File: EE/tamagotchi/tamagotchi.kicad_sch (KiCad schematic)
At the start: 0 parts

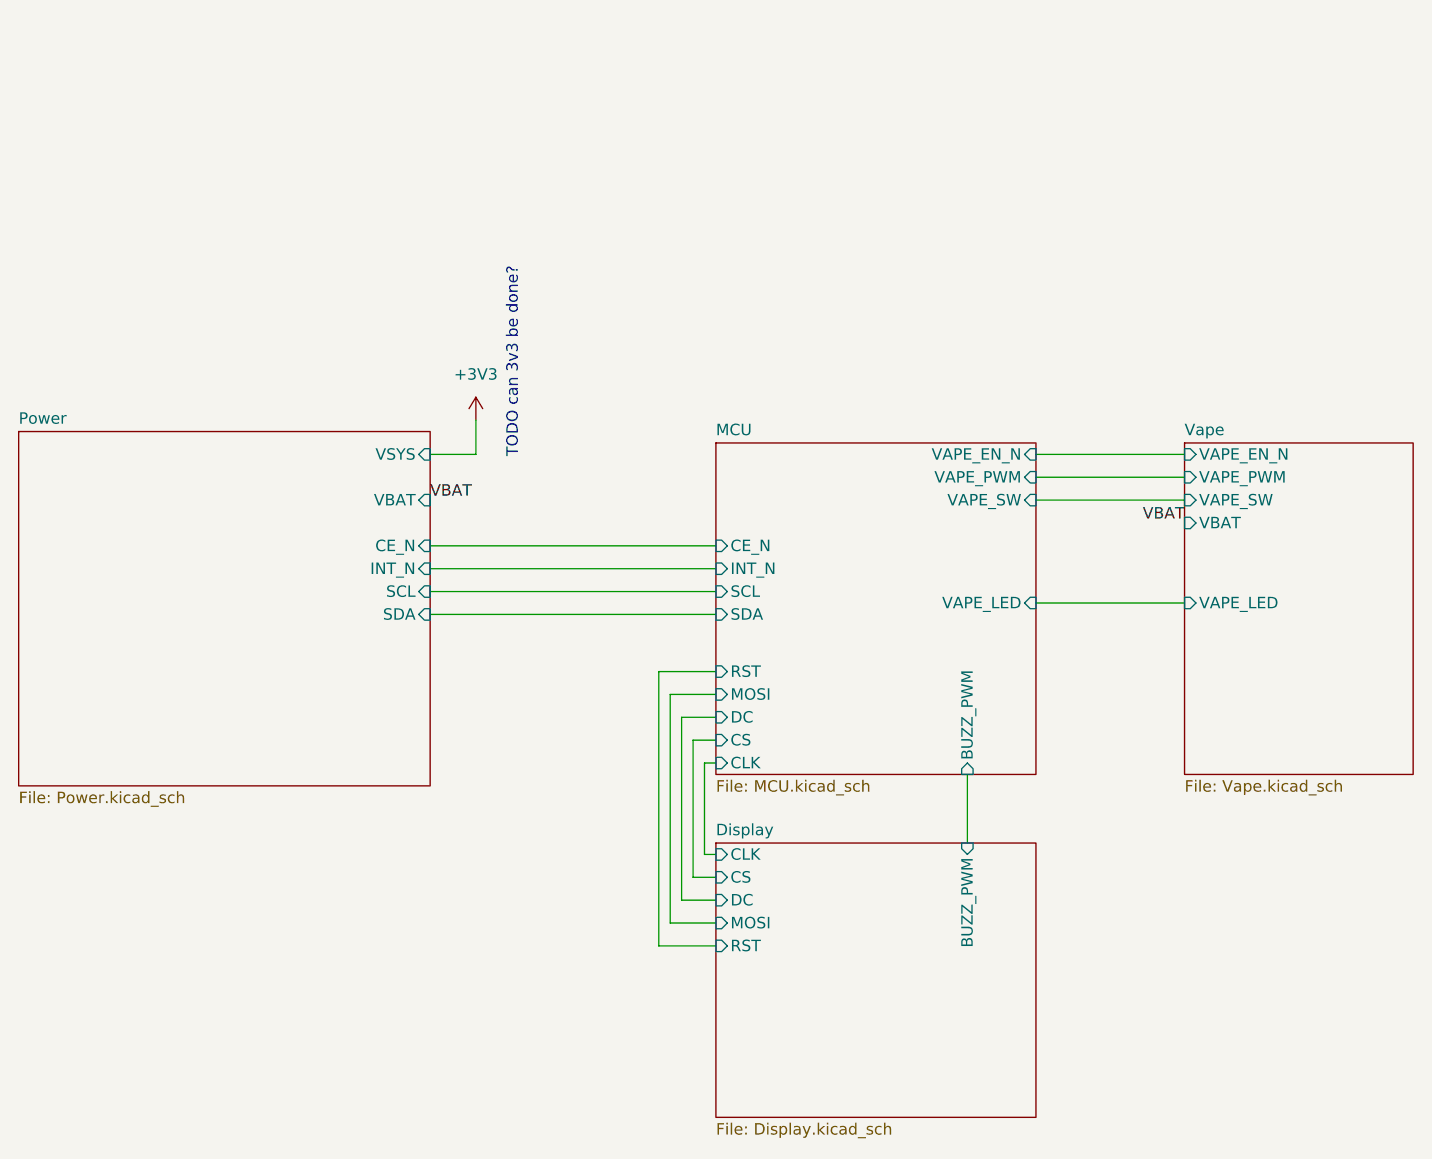
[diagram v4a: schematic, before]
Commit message: Added pressure sensor. Re laid out board
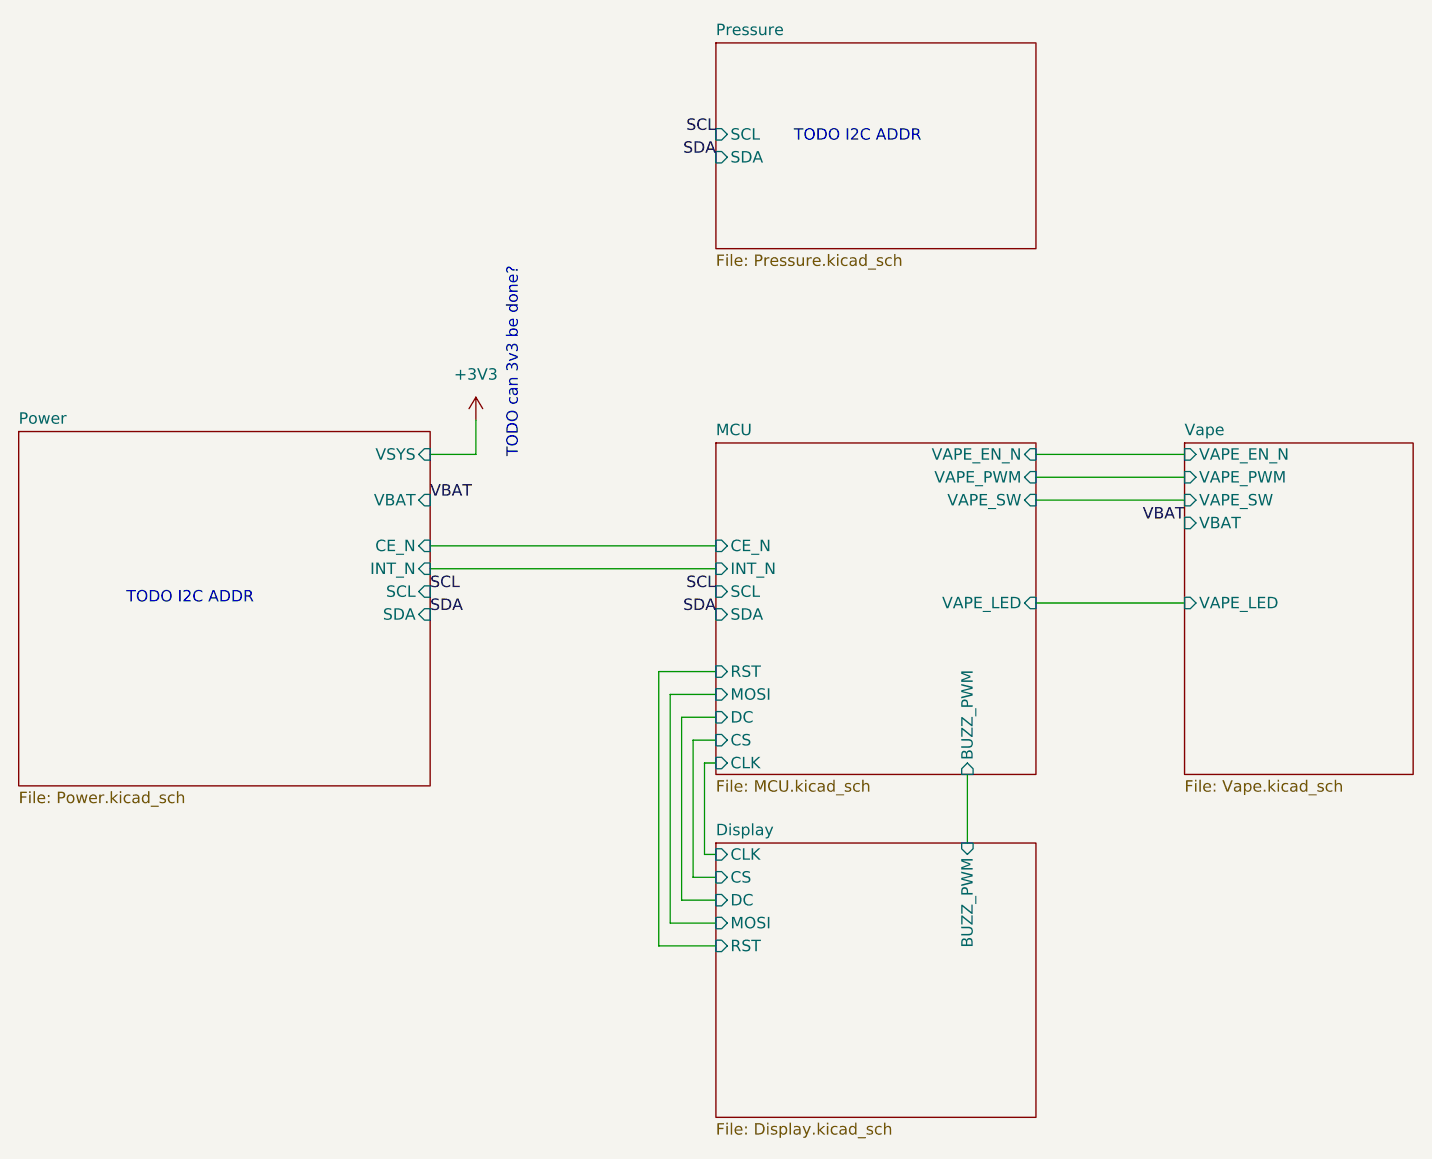
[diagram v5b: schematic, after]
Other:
- added sheet Pressure (Pressure.kicad_sch)
- note added: "TODO I2C ADDR"
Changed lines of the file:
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@@
 	(generator_version "9.0")
 	(paper "A4")
+	(text "TODO I2C ADDR"
+		(exclude_from_sim no)
+		(at 145.288 56.134 0)
+		(effects
+			(font
+				(size 1.27 1.27)
+			)
+		)
+	)
 	(text "TODO can 3v3 be done?"
 		(exclude_from_sim no)
@@
 		)
 	)
+	(text "TODO I2C ADDR"
+		(exclude_from_sim no)
+		(at 71.12 107.442 0)
+		(effects
+			(font
+				(size 1.27 1.27)
+			)
+		)
+	)
 	(wire
 		(pts
@@
 	(wire
 		(pts
-			(xy 97.79 106.68) (xy 129.54 106.68)
-		)
-		(stroke
-			(width 0)
-			(type default)
-		)
-	)
-	(wire
-		(pts
 			(xy 128.27 125.73) (xy 129.54 125.73)
 		)
@@
 	(wire
 		(pts
-			(xy 97.79 109.22) (xy 129.54 109.22)
-		)
-		(stroke
-			(width 0)
-			(type default)
-		)
-	)
-	(wire
-		(pts
 			(xy 97.79 104.14) (xy 129.54 104.14)
 		)
@@
 			(width 0)
 			(type default)
+		)
+	)
+	(label "SCL"
+		(at 97.79 106.68 0)
+		(effects
+			(font
+				(size 1.27 1.27)
+			)
+			(justify left bottom)
 		)
 	)
@@
 		)
 	)
+	(label "SDA"
+		(at 97.79 109.22 0)
+		(effects
+			(font
+				(size 1.27 1.27)
+			)
+			(justify left bottom)
+		)
+	)
 	(label "VBAT"
 		(at 181.61 99.06 180)
+		(effects
+			(font
+				(size 1.27 1.27)
+			)
+			(justify right bottom)
+		)
+	)
+	(label "SDA"
+		(at 129.54 58.42 180)
+		(effects
+			(font
+				(size 1.27 1.27)
+			)
+			(justify right bottom)
+		)
+	)
+	(label "SCL"
+		(at 129.54 106.68 180)
+		(effects
+			(font
+				(size 1.27 1.27)
+			)
+			(justify right bottom)
+		)
+	)
+	(label "SCL"
+		(at 129.54 55.88 180)
+		(effects
+			(font
+				(size 1.27 1.27)
+			)
+			(justify right bottom)
+		)
+	)
+	(label "SDA"
+		(at 129.54 109.22 180)
 		(effects
 			(font
@@
 				)
 			)
+		)
+	)
+	(sheet
+		(at 129.54 45.72)
+		(size 35.56 22.86)
+		(exclude_from_sim no)
+		(in_bom yes)
+		(on_board yes)
+		(dnp no)
+		(fields_autoplaced yes)
+		(stroke
+			(width 0.1524)
+			(type solid)
+		)
+		(fill
+			(color 0 0 0 0.0000)
+		)
+		(property "Sheetname" "Pressure"
+			(at 129.54 45.0084 0)
+			(effects
+				(font
+					(size 1.27 1.27)
+				)
+				(justify left bottom)
+			)
+		)
+		(property "Sheetfile" "Pressure.kicad_sch"
+			(at 129.54 69.1646 0)
+			(effects
+				(font
+					(size 1.27 1.27)
+				)
+				(justify left top)
+			)
+		)
+		(pin "SCL" input
+			(at 129.54 55.88 180)
+			(effects
+				(font
+					(size 1.27 1.27)
+				)
+				(justify left)
+			)
+		)
+		(pin "SDA" input
+			(at 129.54 58.42 180)
+			(effects
+				(font
+					(size 1.27 1.27)
+				)
+				(justify left)
+			)
+		)
+		(instances
+			(project "tamagotchi"
+				(path "/47ffaef6-4682-4a87-a393-bad1a10963be"
+					(page "6")
+				)
+			)
